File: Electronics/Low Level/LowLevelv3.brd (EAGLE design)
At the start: 116.8 x 69.8 mm, 66 parts, among them IC1_2515 MCP2515, IC2_2551 MCP2551DIL08, IC3_4802 MCP4802, Q1 16MHz, T1 2N3904, T2 2N3904, X1 284512-4, X3 Motor, X4 CLICK

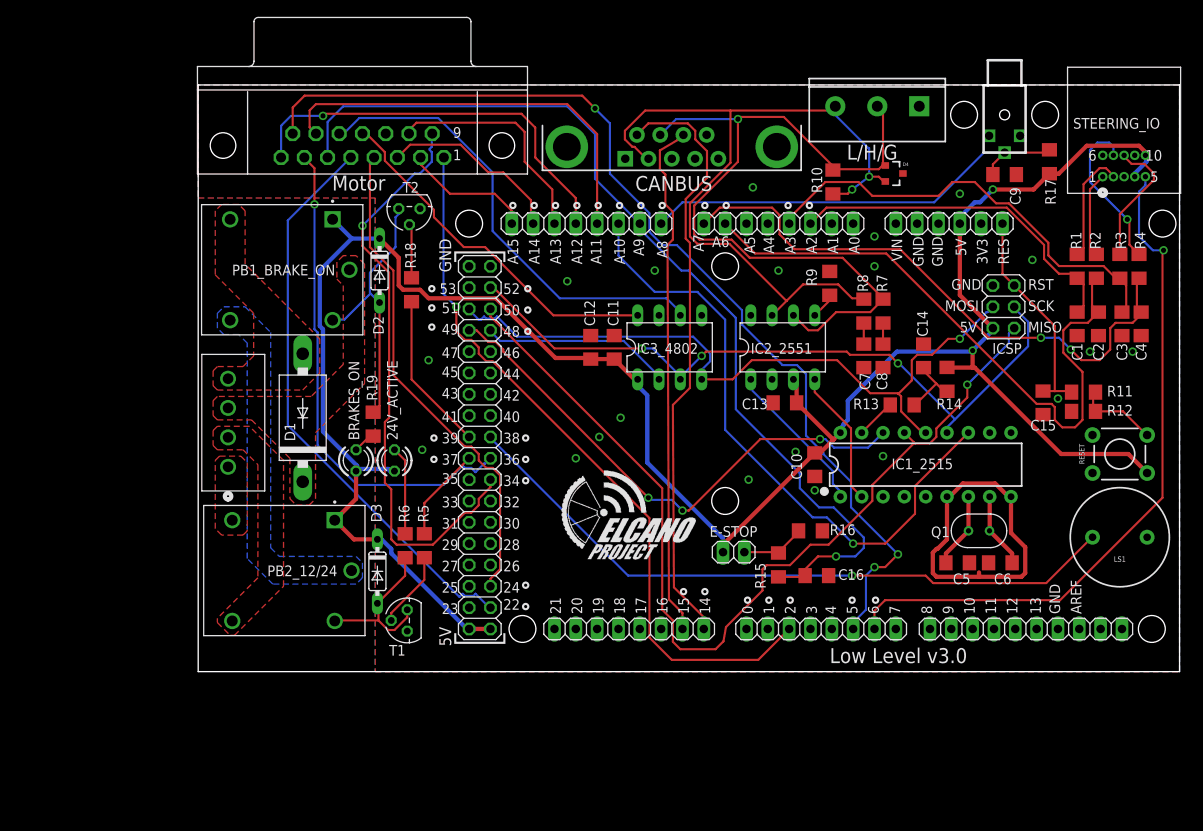
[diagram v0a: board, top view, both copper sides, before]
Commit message: LLBv3 corrections
Fixed silk-via overlapping regions.
Fixed reset button schematic/wiring, now connects reset to ground.
Swapped CAN differential pair pinout by fixing the part in the library and re-routing the board.
Moved some surface mount parts to better propagate the ground plane.

Added on-silkscreen documentation for CAN and relay pinouts.
Added power-OK led and its resistor.
Changed board outline, reduced area and added two corner cuts.
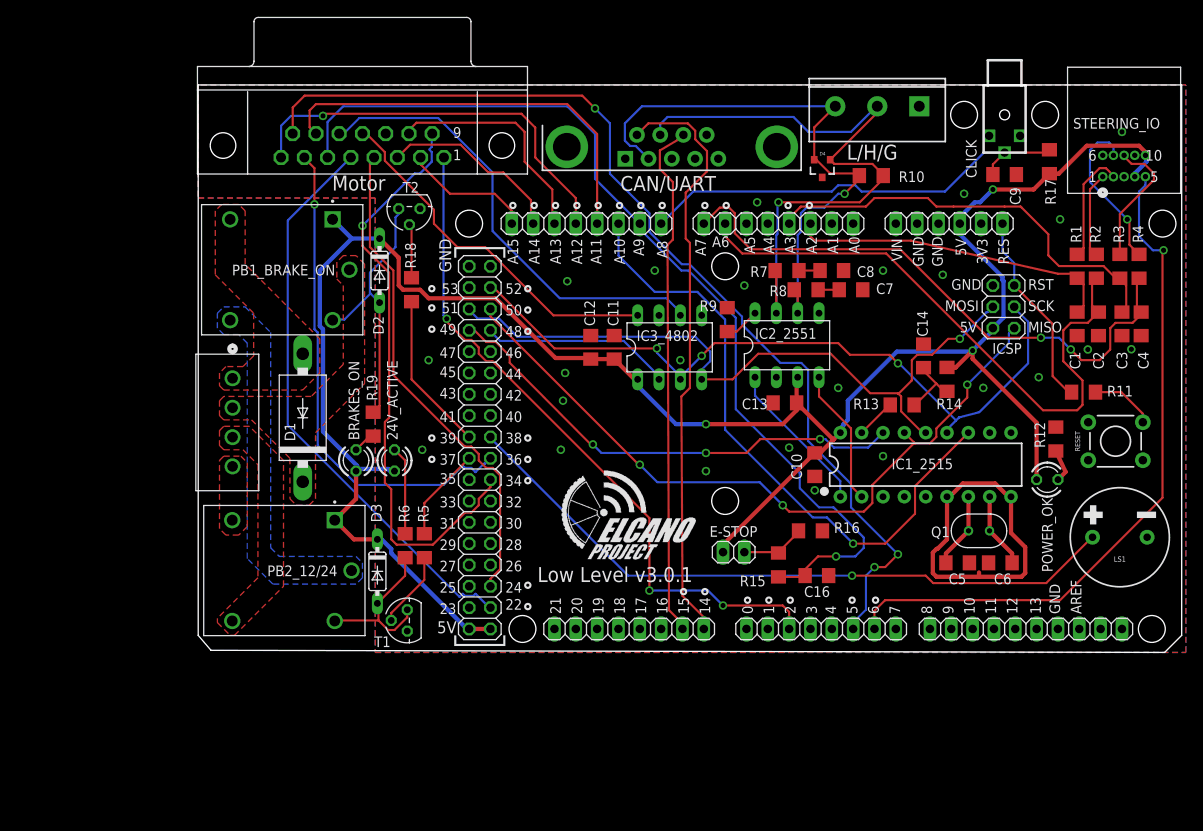
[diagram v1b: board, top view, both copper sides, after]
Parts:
- removed C15: 1uF, resistor:C1206
- added POWER_OK: (no value), led:LED3MM
- ICSP: value ICSP -> 2x3
- R12: value 10k -> 1K
- moved R9 12.9 mm to (63.0, 41.9)
- moved R7 12.4 mm to (70.1, 47.8), turned to 180 degrees
- moved C8 11.8 mm to (75.4, 47.8), turned to 0 degrees
- moved X1 10.6 mm to (4.09, 34.9), turned to 270 degrees
- moved D4 8.53 mm to (74.3, 59.9), turned to 180 degrees
- moved C7 8.02 mm to (77.7, 45.5), turned to 0 degrees
- moved R8 7.31 mm to (72.4, 45.5), turned to 180 degrees
- moved R12 4.67 mm to (102.1, 27.7), turned to 270 degrees
- moved R10 4.64 mm to (80.1, 59.1), turned to 0 degrees
- moved RESET 1.61 mm to (109.2, 27.4)
- moved IC2_2551 0.57 mm to (70.1, 38.9)
- renumbered CANBUS to CAN/UART
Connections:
- new net N$11: POWER_OK.K, R12.2
- net 12V: now also X1.4; no longer X1.1
- net 24V: now also X1.3; no longer X1.2
- net 5V: now also POWER_OK.A; no longer RESET.1
- net CANH: now also IC2_2551.7; no longer IC2_2551.6
- net CANL: now also IC2_2551.6; no longer IC2_2551.7
- net GND: now also R12.1, RESET.1; no longer C15.2, R12.2
- net N$1: no longer R12.1
- net N$14: now also IC2_2551.8; no longer IC2_2551.5
- net RESET: no longer C15.1
- net SOLENOID_COMMON: now also X1.1; no longer X1.4
- net SOLENOID_OUT: now also X1.2; no longer X1.3
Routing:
- net MISO: track 112.7 -> 87.2 mm, vias 1 -> 3
- net CANL: track 93.3 -> 69.3 mm, vias 2 -> 1
- net CANH: track 93.1 -> 77.9 mm
- net 5V: track 268.1 -> 259.1 mm, vias 2 -> 3
- net CAN_SS: track 63.0 -> 57.7 mm
- net BRAKE_PWM: track 87.5 -> 82.3 mm, vias 1 -> 3
- net N$11: track 0.00 -> 4.04 mm
- net L_SENSE: track 42.0 -> 39.1 mm
- net L_RTN_GND: track 75.1 -> 72.4 mm
- net N$1: track 10.2 -> 7.72 mm
- net R_SENSE: track 53.3 -> 51.0 mm
- net RESET: track 26.0 -> 23.7 mm
- net SCK: track 84.3 -> 86.5 mm
- net N$14: track 3.12 -> 4.21 mm
- net TX3: track 71.4 -> 70.5 mm
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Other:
- board size 116.8 x 69.8 mm -> 117.1 x 67.6 mm
- board text added: "12/24"
- board text added: "A"
- board text added: "B"
- board text added: "CAN/UART"
- board text added: "Elcano LLBv3 Ben Rockhold Talor Brady Lucy Okita Alex Xie"
- board text added: "G"
- board text added: "H"
- board text added: "L"
- board text added: "Low Level v3.0.1"
- board text added: "ON/OFF"
- board text added: "X3 - Motor"
- board text removed: "Low Level v3.0"

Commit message: LLBv3.1 changes
Rerouted high-current relay circuit to handle swapped NC/NO pins.
Replaced 10-pin connector with 8-pin RJ45 modular jack. Expensive mistake.
Added debug LED on pin D13.
Added test points for steering header.
Silkscreen and routing corrections.
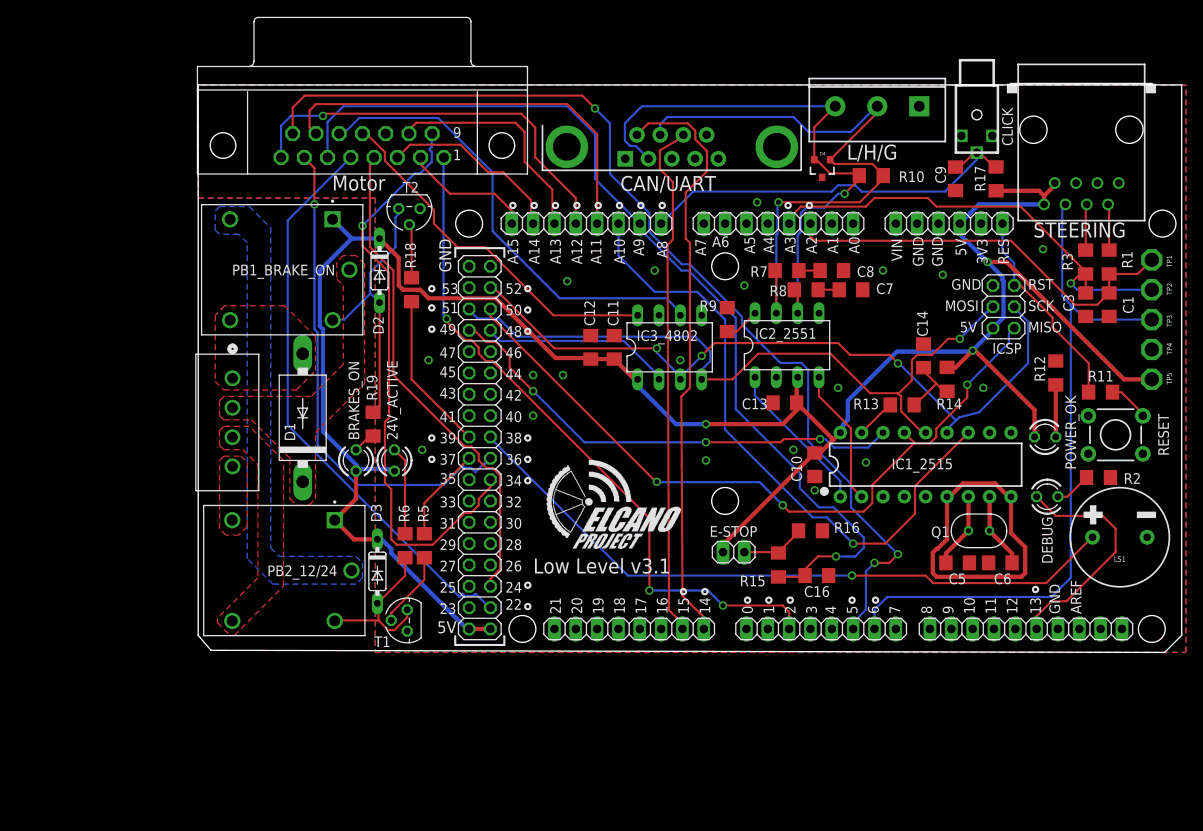
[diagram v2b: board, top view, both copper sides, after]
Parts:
- removed C2, C4: 1uF, resistor:C1206
- removed R4: 4.7K, resistor:R1206
- removed STEERING_IO: 5-104069-4, elcanoParts:CONN_5-104069-4_TYCO
- added DEBUG: (no value), led:LED3MM
- added STEERING: RJ45-8L-B, elcanoParts:RJ45-NO-SHIELD
- added TP1, TP2, TP3, TP4, TP5: PTR1PAD1-17, testpad:P1-17
- R2: value 4.7K -> 1K
- moved R2 25.1 mm to (107.2, 23.1), turned to 180 degrees
- moved R12 7.87 mm to (102.1, 35.6)
- moved R17 6.67 mm to (95.0, 58.7)
- moved C9 5.86 mm to (90.2, 58.7), turned to 270 degrees
- moved POWER_OK 5.09 mm to (100.8, 27.9)
- moved C3 4.89 mm to (105.7, 43.7)
- moved C1 4.44 mm to (108.5, 43.7)
- moved R3 4.10 mm to (105.7, 48.8)
- moved R1 3.84 mm to (108.5, 48.8)
- moved X4 3.30 mm to (92.7, 66.3)
- moved R11 2.03 mm to (107.4, 33.3)
- moved RESET 0.76 mm to (109.2, 28.2)
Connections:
- removed net L_RET: R2.2, STEERING_IO.1
- removed net L_RTN_GND: ADCL.2, C2.1, R2.1
- removed net R_RET: R4.2, STEERING_IO.7
- removed net R_RTN_GND: ADCL.1, C4.1, R4.1
- new net DEBUG_LED: DEBUG.A, DIGITAL_8-13.6
- new net N$5: DEBUG.K, R2.2
- net 12V: now also PB2_12/24.5, X1.3; no longer PB2_12/24.4, X1.4
- net 24V: now also PB2_12/24.4, X1.4; no longer PB2_12/24.5, X1.3
- net 5V: now also STEERING.7, STEERING.8, TP5.TP; no longer STEERING_IO.10, STEERING_IO.4
- net GND: now also R2.1, STEERING.1, STEERING.3, STEERING.5, TP4.TP; no longer C2.2, C4.2, STEERING_IO.3, STEERING_IO.6, STEERING_IO.9
- net L_SENSE: now also TP1.TP
- net L_STR: now also STEERING.2; no longer STEERING_IO.2
- net R_SENSE: now also TP2.TP
- net R_STR: now also STEERING.4; no longer STEERING_IO.8
- net SOLENOID_COMMON: now also PB1_BRAKE_ON.5; no longer PB1_BRAKE_ON.4
- net SOLENOID_POWER: now also PB1_BRAKE_ON.4; no longer PB1_BRAKE_ON.5
- net STEER_SERVO_PWM: now also STEERING.6, TP3.TP; no longer STEERING_IO.5
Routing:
- net L_RTN_GND: track 72.4 -> 0.00 mm
- net R_RTN_GND: track 70.1 -> 0.00 mm, vias 2 -> 0
- net DEBUG_LED: track 0.00 -> 27.8 mm
- net R_RET: track 19.2 -> 0.00 mm, vias 1 -> 0
- net R_STR: track 15.8 -> 5.49 mm
- net L_RET: track 10.2 -> 0.00 mm
- net 5V: track 259.1 -> 269.2 mm
- net L_SENSE: track 39.1 -> 49.1 mm
- net L_STR: track 13.5 -> 5.49 mm
- net WHEELROTATION: track 53.7 -> 48.5 mm
- net N$5: track 0.00 -> 4.35 mm
- net R_SENSE: track 51.0 -> 55.3 mm, vias 0 -> 1
- net N$1: track 7.72 -> 4.92 mm
- net N$11: track 4.04 -> 6.20 mm
- net RESET: track 23.7 -> 24.8 mm
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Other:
- board text added: "Elcano LLB v3.1 Ben Rockhold Talor Brady Lucy Okita Alex Xie"
- board text added: "Low Level v3.1"
- board text removed: "Elcano LLBv3 Ben Rockhold Talor Brady Lucy Okita Alex Xie"
- board text removed: "Low Level v3.0.1"

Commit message: Corrections to silkscreen, added testpoints
Fixed silkscreen errors around the relay terminals, added symbols.
Added testpoints and easily cut traces for steering header ground pins, for future expandability options.
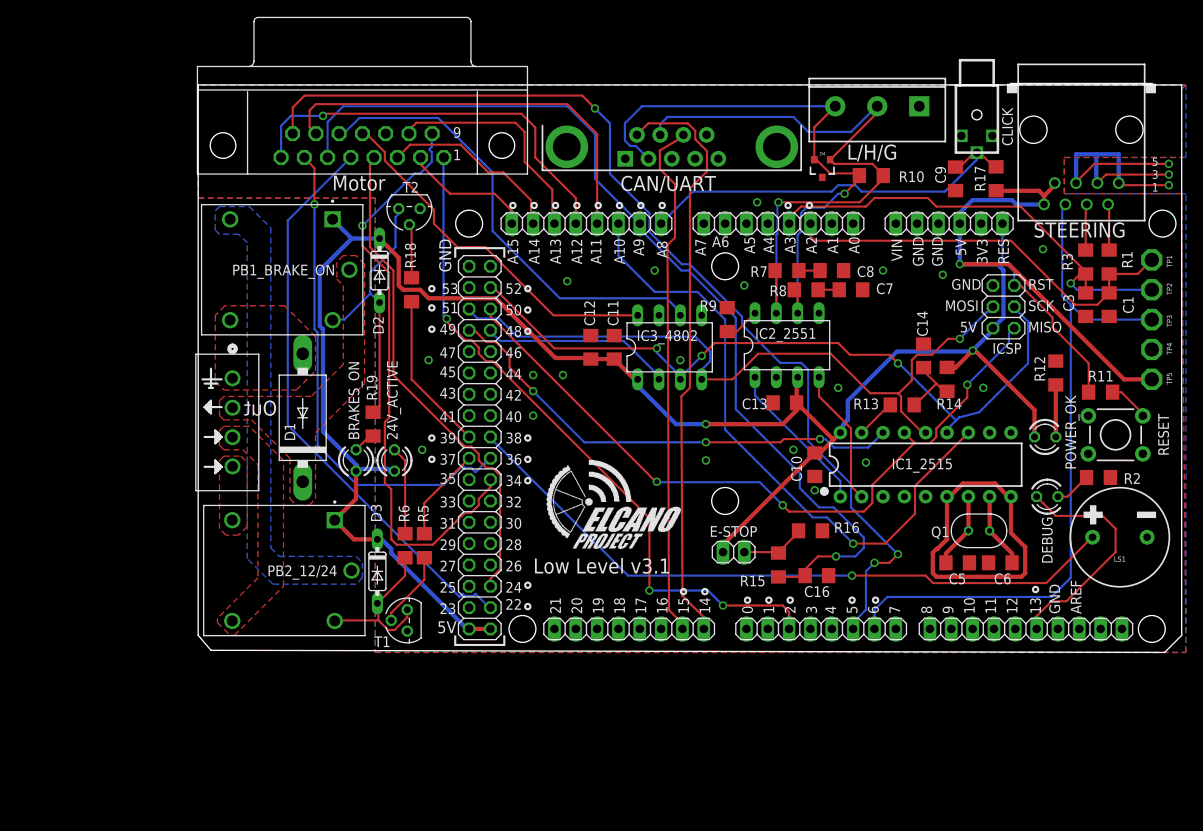
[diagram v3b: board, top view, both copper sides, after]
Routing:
- net GND: track 39.9 -> 82.4 mm, vias 19 -> 22
- net 5V: track 269.2 -> 276.1 mm
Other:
- board text added: "5 3 1"
- board text added: "Out"
- board text removed: "A"
- board text removed: "B"

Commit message: Removed DACB from the DB15 connector. Pin 13 will now be used by the manual throttle as a 5V source.
Also added a pair of test points for DAC channels A & B.
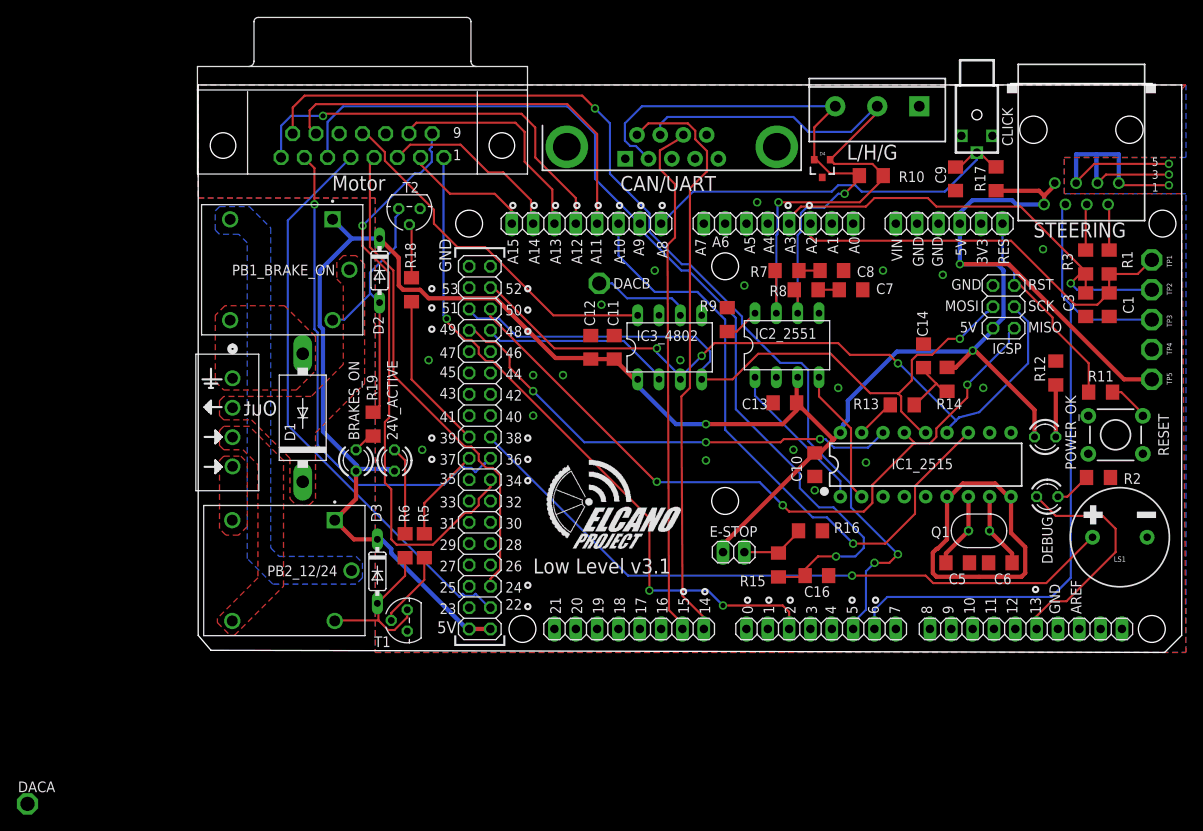
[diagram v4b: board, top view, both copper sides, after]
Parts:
- added DACA, DACB: PTR1PAD1-17, testpad:P1-17
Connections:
- net DACA: now also DACA.TP
- net DACB: now also DACB.TP; no longer X3.13
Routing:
- net DACB: track 55.4 -> 11.8 mm
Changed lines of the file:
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@@
 <attribute name="VALUE" x="113.284" y="22.86" size="0.635" layer="27" rot="R180"/>
+</element>
+<element name="DACB" library="testpad" library_urn="urn:adsk.eagle:library:385" package="P1-17" package3d_urn="urn:adsk.eagle:package:27949/1" value="PTR1PAD1-17" x="47.752" y="46.228" smashed="yes">
+<attribute name="NAME" x="49.403" y="45.593" size="1.27" layer="25" ratio="10"/>
+<attribute name="TP_SIGNAL_NAME" value="" x="47.752" y="46.228" size="1.778" layer="27" display="off"/>
+<attribute name="VALUE" x="47.752" y="44.704" size="0.0254" layer="27"/>
+</element>
+<element name="DACA" library="testpad" library_urn="urn:adsk.eagle:library:385" package="P1-17" package3d_urn="urn:adsk.eagle:package:27949/1" value="PTR1PAD1-17" x="-20.32" y="-15.748" smashed="yes">
+<attribute name="NAME" x="-21.463" y="-14.351" size="1.27" layer="25" ratio="10"/>
+<attribute name="TP_SIGNAL_NAME" value="" x="-21.59" y="-18.923" size="1" layer="37"/>
+<attribute name="VALUE" x="-20.32" y="-15.748" size="0.0254" layer="27"/>
 </element>
 </elements>
@@
 <via x="43.434" y="35.306" extent="1-16" drill="0.6096"/>
 <via x="39.878" y="30.48" extent="1-16" drill="0.6096"/>
-<via x="43.942" y="46.482" extent="1-16" drill="0.6096"/>
+<via x="48.006" y="43.688" extent="1-16" drill="0.6096"/>
 <via x="66.548" y="55.88" extent="1-16" drill="0.6096"/>
 <via x="39.878" y="35.306" extent="1-16" drill="0.6096"/>
@@
 <wire x1="19.558" y1="64.008" x2="20.066" y2="64.008" width="0.254" layer="1"/>
 <wire x1="19.558" y1="64.008" x2="19.558" y2="64.0563" width="0.254" layer="1"/>
+<contactref element="DACA" pad="TP"/>
+<wire x1="-20.32" y1="-15.748" x2="30.861" y2="50.546" width="0" layer="19" extent="1-1"/>
 </signal>
 <signal name="DACB">
-<contactref element="X3" pad="13"/>
 <contactref element="IC3_4802" pad="6"/>
-<wire x1="57.404" y1="42.799" x2="57.404" y2="42.418" width="0.254" layer="16"/>
-<wire x1="55.753" y1="44.45" x2="57.404" y2="42.799" width="0.254" layer="16"/>
-<wire x1="43.053" y1="44.45" x2="55.753" y2="44.45" width="0.254" layer="16"/>
-<wire x1="35.052" y1="52.451" x2="43.053" y2="44.45" width="0.254" layer="16"/>
-<wire x1="35.052" y1="59.436" x2="35.052" y2="52.451" width="0.254" layer="16"/>
-<wire x1="28.575" y1="65.913" x2="35.052" y2="59.436" width="0.254" layer="16"/>
-<wire x1="19.177" y1="65.913" x2="28.575" y2="65.913" width="0.254" layer="16"/>
-<wire x1="19.177" y1="65.913" x2="17.3203" y2="64.0563" width="0.254" layer="16"/>
-<wire x1="16.7894" y1="64.0563" x2="17.3203" y2="64.0563" width="0.254" layer="16"/>
+<wire x1="57.404" y1="42.418" x2="57.404" y2="43.434" width="0.254" layer="16"/>
+<wire x1="56.388" y1="44.45" x2="51.054" y2="44.45" width="0.254" layer="16"/>
+<wire x1="51.054" y1="44.45" x2="49.276" y2="46.228" width="0.254" layer="16"/>
+<wire x1="49.276" y1="46.228" x2="47.752" y2="46.228" width="0.254" layer="16"/>
+<wire x1="57.404" y1="43.434" x2="56.388" y2="44.45" width="0.254" layer="16"/>
+<contactref element="DACB" pad="TP"/>
 </signal>
 <signal name="WATCHDOG">

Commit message: Minor update to high current traces to increase surface area
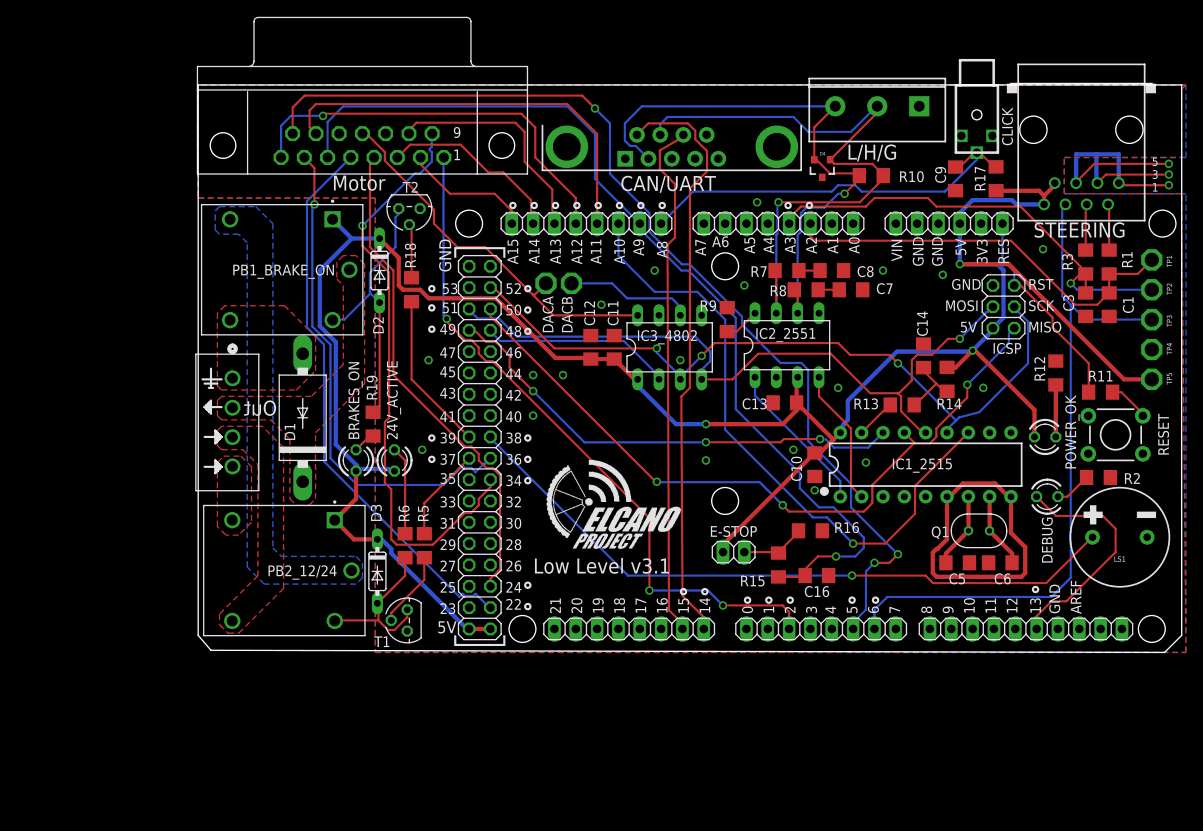
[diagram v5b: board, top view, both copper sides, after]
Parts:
- moved DACA 87.5 mm to (41.4, 46.2)
- moved DACB 3.30 mm to (44.5, 46.2)
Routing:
- net DACB: track 11.8 -> 15.1 mm
- net DACA: track 43.3 -> 45.5 mm
- net REGEN_ACTIVE: track 68.6 -> 66.8 mm
